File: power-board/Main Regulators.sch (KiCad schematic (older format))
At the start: 19 parts, among them U1 LMZ23610

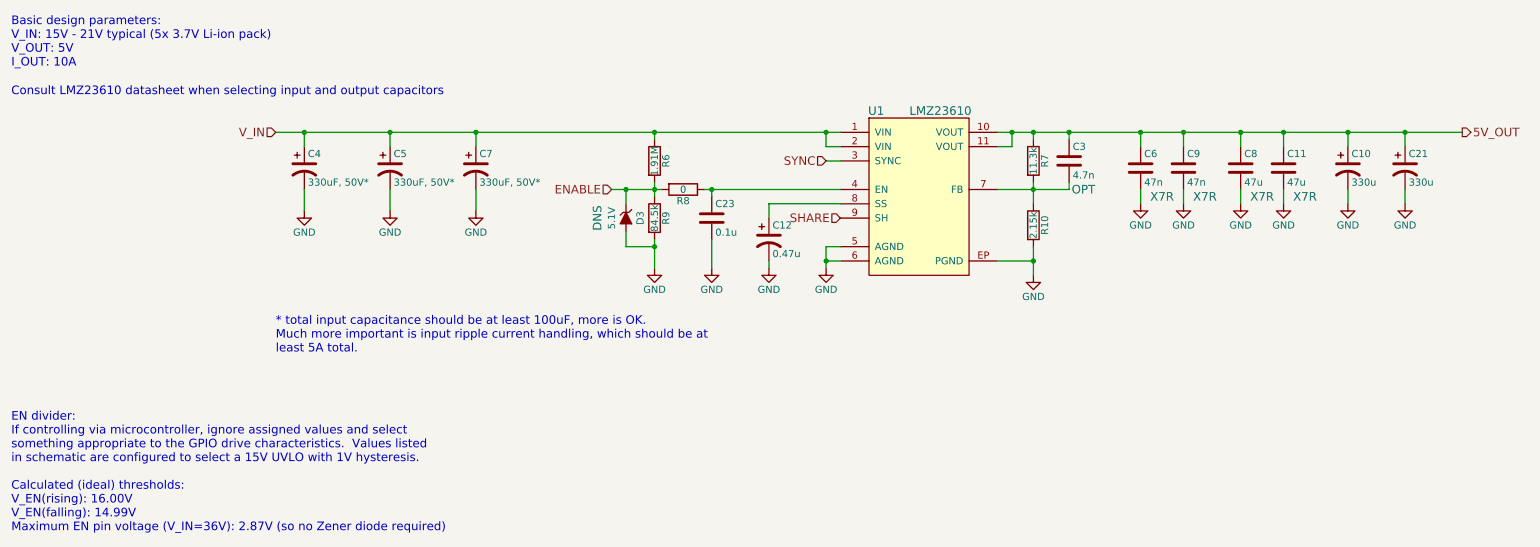
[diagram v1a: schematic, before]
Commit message: switched to XMEGA A4U
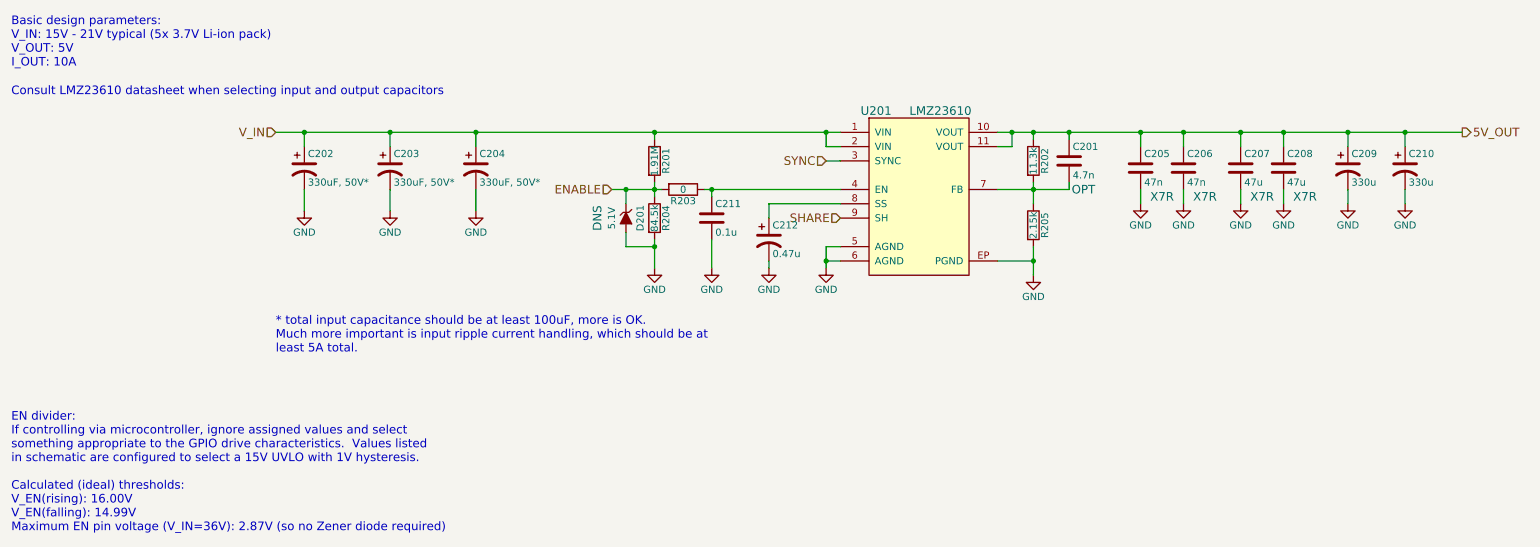
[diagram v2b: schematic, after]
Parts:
- renumbered C3 to C201, C4 to C202, C5 to C203, C7 to C204, C6 to C205, C9 to C206, C8 to C207, C11 to C208, C10 to C209, C21 to C210, C23 to C211, C12 to C212, D3 to D201, R6 to R201, R7 to R202, R8 to R203, R9 to R204, R10 to R205, U1 to U201
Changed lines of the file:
@@
 $Descr A4 11693 8268
 encoding utf-8
-Sheet 2 10
+Sheet 2 11
 Title ""
 Date ""
@@
 $EndDescr
 $Comp
-L LMZ23610 U1
+L LMZ23610 U201
 U 1 1 5934B66C
 P 6600 1300
-F 0 "U1" H 6650 1350 60  0000 C CNN
+F 0 "U201" H 6650 1350 60  0000 C CNN
 F 1 "LMZ23610" H 7100 1350 60  0000 C CNN
 F 2 "" H 6900 1050 60  0001 C CNN
@@
 5V_OUT
 $Comp
-L GND #PWR8
+L GND #PWR01
 U 1 1 5934D6B1
 P 3250 1950
-F 0 "#PWR8" H 3250 1700 50  0001 C CNN
+F 0 "#PWR01" H 3250 1700 50  0001 C CNN
 F 1 "GND" H 3250 1800 50  0000 C CNN
 F 2 "" H 3250 1950 50  0001 C CNN
@@
 $EndComp
 $Comp
-L GND #PWR9
+L GND #PWR02
 U 1 1 5934D6B7
 P 3850 1950
-F 0 "#PWR9" H 3850 1700 50  0001 C CNN
+F 0 "#PWR02" H 3850 1700 50  0001 C CNN
 F 1 "GND" H 3850 1800 50  0000 C CNN
 F 2 "" H 3850 1950 50  0001 C CNN
@@
 ENABLE
 $Comp
-L R R10
+L R R205
 U 1 1 5934DCA9
 P 7750 2050
-F 0 "R10" V 7830 2050 50  0000 C CNN
+F 0 "R205" V 7830 2050 50  0000 C CNN
 F 1 "2.15k" V 7750 2050 50  0000 C CNN
 F 2 "" V 7680 2050 50  0000 C CNN
@@
 $EndComp
 $Comp
-L R R7
+L R R202
 U 1 1 5934DCDA
 P 7750 1600
-F 0 "R7" V 7830 1600 50  0000 C CNN
+F 0 "R202" V 7830 1600 50  0000 C CNN
 F 1 "11.3k" V 7750 1600 50  0000 C CNN
 F 2 "" V 7680 1600 50  0000 C CNN
@@
 $EndComp
 $Comp
-L GND #PWR14
+L GND #PWR03
 U 1 1 5934DDA1
 P 7750 2400
-F 0 "#PWR14" H 7750 2150 50  0001 C CNN
+F 0 "#PWR03" H 7750 2150 50  0001 C CNN
 F 1 "GND" H 7750 2250 50  0000 C CNN
 F 2 "" H 7750 2400 50  0000 C CNN
@@
 $EndComp
 $Comp
-L GND #PWR13
+L GND #PWR04
 U 1 1 5934DDBF
 P 6300 2350
-F 0 "#PWR13" H 6300 2100 50  0001 C CNN
+F 0 "#PWR04" H 6300 2100 50  0001 C CNN
 F 1 "GND" H 6300 2200 50  0000 C CNN
 F 2 "" H 6300 2350 50  0000 C CNN
@@
 Basic design parameters:\nV_IN: 15V - 21V typical (5x 3.7V Li-ion pack)\nV_OUT: 5V\nI_OUT: 10A
 $Comp
-L R R6
+L R R201
 U 1 1 5934E7ED
 P 5100 1600
-F 0 "R6" V 5180 1600 50  0000 C CNN
+F 0 "R201" V 5180 1600 50  0000 C CNN
 F 1 "1.91M" V 5100 1600 50  0000 C CNN
 F 2 "" V 5030 1600 50  0000 C CNN
@@
 $EndComp
 $Comp
-L R R9
+L R R204
 U 1 1 5934E882
 P 5100 2000
-F 0 "R9" V 5180 2000 50  0000 C CNN
+F 0 "R204" V 5180 2000 50  0000 C CNN
 F 1 "84.5k" V 5100 2000 50  0000 C CNN
 F 2 "" V 5030 2000 50  0000 C CNN
@@
 $EndComp
 $Comp
-L R R8
+L R R203
 U 1 1 5934E8C2
 P 5300 1800
-F 0 "R8" V 5380 1800 50  0000 C CNN
+F 0 "R203" V 5380 1800 50  0000 C CNN
 F 1 "0" V 5300 1800 50  0000 C CNN
 F 2 "" V 5230 1800 50  0000 C CNN
@@
 $EndComp
 $Comp
-L ZENERsmall D3
+L ZENERsmall D201
 U 1 1 5934E900
 P 4900 2000
-F 0 "D3" H 4900 2100 50  0000 C CNN
+F 0 "D201" H 4900 2100 50  0000 C CNN
 F 1 "5.1V" H 4900 1900 50  0000 C CNN
 F 2 "" H 4900 2000 50  0000 C CNN
@@
 	6300 1600 6400 1600
 $Comp
-L CP1 C12
+L CP1 C212
 U 1 1 5934EDD9
 P 5900 2150
-F 0 "C12" H 5925 2250 50  0000 L CNN
+F 0 "C212" H 5925 2250 50  0000 L CNN
 F 1 "0.47u" H 5925 2050 50  0000 L CNN
 F 2 "" H 5900 2150 50  0000 C CNN
@@
 	5900 2300 5900 2350
 $Comp
-L GND #PWR12
+L GND #PWR05
 U 1 1 5934EEE1
 P 5900 2350
-F 0 "#PWR12" H 5900 2100 50  0001 C CNN
+F 0 "#PWR05" H 5900 2100 50  0001 C CNN
 F 1 "GND" H 5900 2200 50  0000 C CNN
 F 2 "" H 5900 2350 50  0000 C CNN
@@
 Connection ~ 5100 2200
 $Comp
-L GND #PWR10
+L GND #PWR06
 U 1 1 5934F49E
 P 5100 2350
-F 0 "#PWR10" H 5100 2100 50  0001 C CNN
+F 0 "#PWR06" H 5100 2100 50  0001 C CNN
 F 1 "GND" H 5100 2200 50  0000 C CNN
 F 2 "" H 5100 2350 50  0000 C CNN
@@
 Connection ~ 4900 1800
 $Comp
-L C C6
+L C C205
 U 1 1 5934F7F0
 P 8500 1650
-F 0 "C6" H 8525 1750 50  0000 L CNN
+F 0 "C205" H 8525 1750 50  0000 L CNN
 F 1 "47n" H 8525 1550 50  0000 L CNN
 F 2 "" H 8538 1500 50  0001 C CNN
@@
 EN divider:\nIf controlling via microcontroller, ignore assigned values and select\nsomething appropriate to the GPIO drive characteristics.  Values listed\nin schematic are configured to select a 15V UVLO with 1V hysteresis.\n\nCalculated (ideal) thresholds:\nV_EN(rising): 16.00V\nV_EN(falling): 14.99V\nMaximum EN pin voltage (V_IN=36V): 2.87V (so no Zener diode required)
 $Comp
-L C C3
+L C C201
 U 1 1 59350638
 P 8000 1600
-F 0 "C3" H 8025 1700 50  0000 L CNN
+F 0 "C201" H 8025 1700 50  0000 L CNN
 F 1 "4.7n" H 8025 1500 50  0000 L CNN
 F 2 "" H 8038 1450 50  0000 C CNN
@@
 Consult LMZ23610 datasheet when selecting input and output capacitors
 $Comp
-L GND #PWR1
+L GND #PWR07
 U 1 1 59350B83
 P 8500 1900
-F 0 "#PWR1" H 8500 1650 50  0001 C CNN
+F 0 "#PWR07" H 8500 1650 50  0001 C CNN
 F 1 "GND" H 8500 1750 50  0000 C CNN
 F 2 "" H 8500 1900 50  0000 C CNN
@@
 $EndComp
 $Comp
-L GND #PWR6
+L GND #PWR08
 U 1 1 59350BB5
 P 10350 1900
-F 0 "#PWR6" H 10350 1650 50  0001 C CNN
+F 0 "#PWR08" H 10350 1650 50  0001 C CNN
 F 1 "GND" H 10350 1750 50  0000 C CNN
 F 2 "" H 10350 1900 50  0000 C CNN
@@
 	8500 1900 8500 1800
 $Comp
-L CP1 C10
+L CP1 C209
 U 1 1 59350F51
 P 9950 1650
-F 0 "C10" H 9975 1750 50  0000 L CNN
+F 0 "C209" H 9975 1750 50  0000 L CNN
 F 1 "330u" H 9975 1550 50  0000 L CNN
 F 2 "" H 9950 1650 50  0000 C CNN
@@
 $EndComp
 $Comp
-L GND #PWR5
+L GND #PWR09
 U 1 1 59350F57
 P 9950 1900
-F 0 "#PWR5" H 9950 1650 50  0001 C CNN
+F 0 "#PWR09" H 9950 1650 50  0001 C CNN
 F 1 "GND" H 9950 1750 50  0000 C CNN
 F 2 "" H 9950 1900 50  0000 C CNN
@@
 	9950 1500 9950 1400
 $Comp
-L GND #PWR2
+L GND #PWR010
 U 1 1 59351066
 P 8800 1900
-F 0 "#PWR2" H 8800 1650 50  0001 C CNN
+F 0 "#PWR010" H 8800 1650 50  0001 C CNN
 F 1 "GND" H 8800 1750 50  0000 C CNN
 F 2 "" H 8800 1900 50  0000 C CNN
@@
 	8800 1900 8800 1800
 $Comp
-L C C8
+L C C207
 U 1 1 593510C1
 P 9200 1650
-F 0 "C8" H 9225 1750 50  0000 L CNN
+F 0 "C207" H 9225 1750 50  0000 L CNN
 F 1 "47u" H 9225 1550 50  0000 L CNN
 F 2 "" H 9238 1500 50  0001 C CNN
@@
 $EndComp
 $Comp
-L GND #PWR3
+L GND #PWR011
 U 1 1 593510C7
 P 9200 1900
-F 0 "#PWR3" H 9200 1650 50  0001 C CNN
+F 0 "#PWR011" H 9200 1650 50  0001 C CNN
 F 1 "GND" H 9200 1750 50  0000 C CNN
 F 2 "" H 9200 1900 50  0000 C CNN
@@
 	9200 1900 9200 1800
 $Comp
-L GND #PWR4
+L GND #PWR012
 U 1 1 59351182
 P 9500 1900
-F 0 "#PWR4" H 9500 1650 50  0001 C CNN
+F 0 "#PWR012" H 9500 1650 50  0001 C CNN
 F 1 "GND" H 9500 1750 50  0000 C CNN
 F 2 "" H 9500 1900 50  0000 C CNN
@@
 Connection ~ 9950 1400
 $Comp
-L C C23
+L C C211
 U 1 1 593AB48E
 P 5500 2000
-F 0 "C23" H 5525 2100 50  0000 L CNN
+F 0 "C211" H 5525 2100 50  0000 L CNN
 F 1 "0.1u" H 5525 1900 50  0000 L CNN
 F 2 "" H 5538 1850 50  0001 C CNN
@@
 	5500 2150 5500 2350
 $Comp
-L GND #PWR11
+L GND #PWR013
 U 1 1 593AB816
 P 5500 2350
-F 0 "#PWR11" H 5500 2100 50  0001 C CNN
+F 0 "#PWR013" H 5500 2100 50  0001 C CNN
 F 1 "GND" H 5500 2200 50  0000 C CNN
 F 2 "" H 5500 2350 50  0000 C CNN
@@
 $EndComp
 $Comp
-L CP1 C21
+L CP1 C210
 U 1 1 593A0A87
 P 10350 1650
-F 0 "C21" H 10375 1750 50  0000 L CNN
+F 0 "C210" H 10375 1750 50  0000 L CNN
 F 1 "330u" H 10375 1550 50  0000 L CNN
 F 2 "" H 10350 1650 50  0000 C CNN
@@
 $EndComp
 $Comp
-L C C9
+L C C206
 U 1 1 593ACB4B
 P 8800 1650
-F 0 "C9" H 8825 1750 50  0000 L CNN
+F 0 "C206" H 8825 1750 50  0000 L CNN
 F 1 "47n" H 8825 1550 50  0000 L CNN
 F 2 "" H 8838 1500 50  0001 C CNN
@@
 $EndComp
 $Comp
-L CP1 C5
+L CP1 C203
 U 1 1 593B354D
 P 3250 1650
-F 0 "C5" H 3275 1750 50  0000 L CNN
+F 0 "C203" H 3275 1750 50  0000 L CNN
 F 1 "330uF, 50V*" H 3275 1550 50  0000 L CNN
 F 2 "" H 3250 1650 50  0001 C CNN
@@
 $EndComp
 $Comp
-L CP1 C7
+L CP1 C204
 U 1 1 593B3689
 P 3850 1650
-F 0 "C7" H 3875 1750 50  0000 L CNN
+F 0 "C204" H 3875 1750 50  0000 L CNN
 F 1 "330uF, 50V*" H 3875 1550 50  0000 L CNN
 F 2 "" H 3850 1650 50  0001 C CNN
@@
 $EndComp
 $Comp
-L CP1 C4
+L CP1 C202
 U 1 1 593B36D8
 P 2650 1650
-F 0 "C4" H 2675 1750 50  0000 L CNN
+F 0 "C202" H 2675 1750 50  0000 L CNN
 F 1 "330uF, 50V*" H 2675 1550 50  0000 L CNN
 F 2 "" H 2650 1650 50  0001 C CNN
@@
 	2650 1800 2650 1950
 $Comp
-L GND #PWR7
+L GND #PWR014
 U 1 1 593B3936
 P 2650 1950
-F 0 "#PWR7" H 2650 1700 50  0001 C CNN
+F 0 "#PWR014" H 2650 1700 50  0001 C CNN
 F 1 "GND" H 2650 1800 50  0000 C CNN
 F 2 "" H 2650 1950 50  0001 C CNN
@@
 * total input capacitance should be at least 100uF, more is OK.\nMuch more important is input ripple current handling, which should be at\nleast 5A total.
 $Comp
-L C C11
+L C C208
 U 1 1 593B3E3D
 P 9500 1650
-F 0 "C11" H 9525 1750 50  0000 L CNN
+F 0 "C208" H 9525 1750 50  0000 L CNN
 F 1 "47u" H 9525 1550 50  0000 L CNN
 F 2 "" H 9538 1500 50  0001 C CNN

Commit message: routed board
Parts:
- removed C208: 47u, symbol C
- added C208, C213: 330u, Capacitors_Tantalum_SMD:Tantalum_Case-V_EIA-7343-20_Hand, symbol CP1
- C201: footprint (none) -> Capacitors_SMD:C_0603; MFG (none) -> Samsung; MPN (none) -> CL10B472KB8NNNC; Note OPT -> (none)
- C202, C203, C204: value 330uF, 50V* -> 10uF; footprint (none) -> Capacitors_SMD:C_1210; MFG Panasonic Electronic Components -> TDK Corporation; MPN EEU-FM1H331L -> C3225X7S1H106M250AB; Note (none) -> 50V, Low ESL
- C205, C206, C211, C212: footprint (none) -> Capacitors_SMD:C_0603
- C207: footprint (none) -> Capacitors_SMD:C_0805
- C209, C210: footprint (none) -> Capacitors_Tantalum_SMD:Tantalum_Case-V_EIA-7343-20_Hand; MFG Kemet -> AVX Corporation; MPN A750KK337M1CAAE014 -> TCJD337M006R0025; Note low-ESR -> 6.3V, 0.025 ohm
- D201: footprint (none) -> Diodes_SMD:D_SOD-123
- R201: footprint (none) -> Resistors_SMD:R_0805; MFG Vishay -> Yageo; MPN CRCW06031M91FKEA -> RC0805FR-071M91L
- R202: footprint (none) -> Resistors_SMD:R_0805; MFG Vishay -> Yageo; MPN CRCW060311K3FKEA -> RC0805FR-0711K3L
- R203: footprint (none) -> Resistors_SMD:R_0805
- R204: footprint (none) -> Resistors_SMD:R_0805; MFG Vishay -> Yageo; MPN CRCW060384K5FKEA -> RC0805FR-0784K5L
- R205: footprint (none) -> Resistors_SMD:R_0805; MFG (none) -> Yageo; MPN (none) -> RC0805FR-072K15L
- U201: footprint (none) -> project:TO-PMOD-11
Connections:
- net 5V_OUT: now also C208.1, C213.1; no longer C205.1
- net GND: now also C208.2, C213.2
- net V_IN: now also C205.1
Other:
- note added: "Total input capacitance should be at least 30uF*, more is OK.\nMuch more important is input ripple current handling, which should be at\nleast 5A total.\n\n* to maintain about 250 mV input ripple voltage"
- note removed: "* total input capacitance should be at least 100uF, more is OK.\nMuch more important is input ripple current handling, which should be at\nleast 5A total."
- moved on the sheet: C202, C205, C206, C207, C209, C211, C212, D201, R201, R202, R203, R204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

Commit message: adding more part numbers
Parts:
- R203: MFG (none) -> Yageo; MPN (none) -> RC0805JR-070RL
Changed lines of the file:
@@
 F 2 "Resistors_SMD:R_0805" V 3930 1800 50  0001 C CNN
 F 3 "" H 4000 1800 50  0000 C CNN
+F 4 "Yageo" V 4000 1800 60  0001 C CNN "MFG"
+F 5 "RC0805JR-070RL" V 4000 1800 60  0001 C CNN "MPN"
 	1    4000 1800
 	0    1    1    0
